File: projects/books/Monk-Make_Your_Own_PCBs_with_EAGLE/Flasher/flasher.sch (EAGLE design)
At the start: 10 parts, among them IC1 NE555, J1 1X2-3.5MM

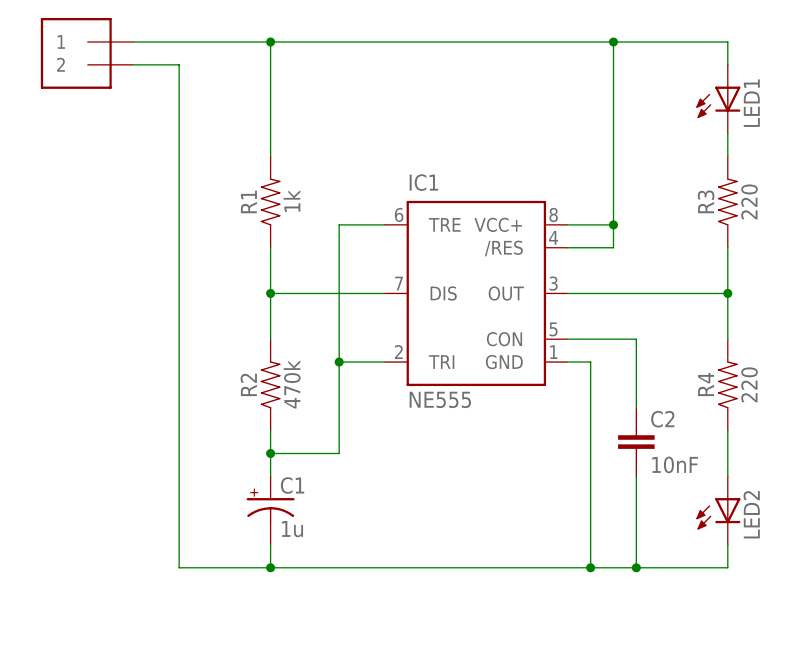
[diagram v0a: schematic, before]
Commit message: Updated flasher schematic
Signed-off-by: Naveed Kawsar <naveedkawsar@outlook.com>
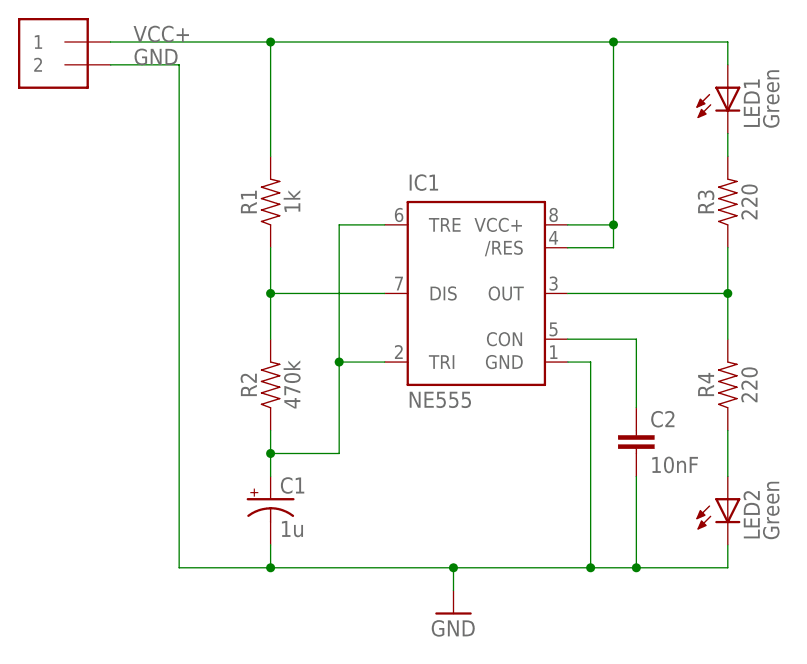
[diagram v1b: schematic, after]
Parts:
- LED1, LED2: value (none) -> Green
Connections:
- net N$5 renamed VCC+
- net N$6 renamed GND
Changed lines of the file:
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@@
 </classes>
 <parts>
-<part name="FRAME1" library="frames" library_urn="urn:adsk.eagle:library:229" deviceset="A4L-LOC" device=""/>
 <part name="R1" library="SparkFun-Resistors" deviceset="1KOHM" device="-HORIZ-1/4W-1%" value="1k"/>
 <part name="R2" library="SparkFun-Resistors" deviceset="RESISTOR" device="AXIAL-0.3" value=" 470k"/>
@@
 <part name="R4" library="SparkFun-Resistors" deviceset="220OHM" device="-0603-1/10W-1%" value="220"/>
 <part name="IC1" library="st-microelectronics" library_urn="urn:adsk.eagle:library:368" deviceset="NE555" device="" package3d_urn="urn:adsk.eagle:package:26829/1"/>
-<part name="LED1" library="led" library_urn="urn:adsk.eagle:library:259" deviceset="LED" device="5MM" package3d_urn="urn:adsk.eagle:package:15799/1"/>
-<part name="LED2" library="led" library_urn="urn:adsk.eagle:library:259" deviceset="LED" device="5MM" package3d_urn="urn:adsk.eagle:package:15799/1"/>
+<part name="LED1" library="led" library_urn="urn:adsk.eagle:library:259" deviceset="LED" device="5MM" package3d_urn="urn:adsk.eagle:package:15799/1" value="Green"/>
+<part name="LED2" library="led" library_urn="urn:adsk.eagle:library:259" deviceset="LED" device="5MM" package3d_urn="urn:adsk.eagle:package:15799/1" value="Green"/>
 <part name="C1" library="resistor" library_urn="urn:adsk.eagle:library:348" deviceset="CPOL-US" device="E2.5-5" package3d_urn="urn:adsk.eagle:package:25841/1" value="1u"/>
 <part name="J1" library="adafruit" deviceset="1X2" device="-3.5MM"/>
 <part name="C2" library="SparkFun-Capacitors" deviceset="10NF" device="-PTH-10MM-10000V-1-%" value="10nF"/>
+<part name="GND1" library="supply1" library_urn="urn:adsk.eagle:library:371" deviceset="GND" device=""/>
+<part name="FRAME1" library="frames" library_urn="urn:adsk.eagle:library:229" deviceset="FRAME_A_L" device=""/>
 </parts>
 <sheets>
@@
 </plain>
 <instances>
-<instance part="FRAME1" gate="G$1" x="-66.04" y="-55.88"/>
 <instance part="R1" gate="G$1" x="43.18" y="48.26" rot="R90"/>
 <instance part="R2" gate="G$1" x="43.18" y="27.94" rot="R90"/>
@@
 <instance part="LED2" gate="G$1" x="93.98" y="15.24"/>
 <instance part="C1" gate="G$1" x="43.18" y="15.24"/>
-<instance part="J1" gate="G$1" x="22.86" y="63.5" rot="MR0"/>
+<instance part="J1" gate="G$1" x="20.32" y="63.5" rot="MR0"/>
 <instance part="C2" gate="G$1" x="83.82" y="20.32"/>
+<instance part="GND1" gate="1" x="63.5" y="2.54"/>
+<instance part="FRAME1" gate="G$1" x="-73.66" y="-71.12"/>
+<instance part="FRAME1" gate="G$2" x="99.06" y="-71.12"/>
 </instances>
 <busses>
@@
 </segment>
 </net>
-<net name="N$6" class="0">
-<segment>
-<pinref part="C1" gate="G$1" pin="-"/>
-<wire x1="43.18" y1="10.16" x2="43.18" y2="7.62" width="0.1524" layer="91"/>
-<wire x1="43.18" y1="7.62" x2="78.74" y2="7.62" width="0.1524" layer="91"/>
-<pinref part="LED2" gate="G$1" pin="C"/>
-<wire x1="78.74" y1="7.62" x2="83.82" y2="7.62" width="0.1524" layer="91"/>
-<wire x1="83.82" y1="7.62" x2="93.98" y2="7.62" width="0.1524" layer="91"/>
-<wire x1="93.98" y1="7.62" x2="93.98" y2="10.16" width="0.1524" layer="91"/>
-<pinref part="IC1" gate="G$1" pin="GND"/>
-<wire x1="76.2" y1="30.48" x2="78.74" y2="30.48" width="0.1524" layer="91"/>
-<wire x1="78.74" y1="30.48" x2="78.74" y2="7.62" width="0.1524" layer="91"/>
-<junction x="78.74" y="7.62"/>
-<pinref part="J1" gate="G$1" pin="2"/>
-<wire x1="27.94" y1="63.5" x2="33.02" y2="63.5" width="0.1524" layer="91"/>
-<wire x1="33.02" y1="63.5" x2="33.02" y2="7.62" width="0.1524" layer="91"/>
-<wire x1="33.02" y1="7.62" x2="43.18" y2="7.62" width="0.1524" layer="91"/>
-<junction x="43.18" y="7.62"/>
-<pinref part="C2" gate="G$1" pin="2"/>
-<wire x1="83.82" y1="17.78" x2="83.82" y2="7.62" width="0.1524" layer="91"/>
-<junction x="83.82" y="7.62"/>
-</segment>
-</net>
 <net name="N$7" class="0">
 <segment>
@@
 </segment>
 </net>
-<net name="N$5" class="0">
+<net name="VCC+" class="0">
 <segment>
 <pinref part="LED1" gate="G$1" pin="A"/>
@@
 <junction x="81.28" y="45.72"/>
 <pinref part="J1" gate="G$1" pin="1"/>
-<wire x1="27.94" y1="66.04" x2="43.18" y2="66.04" width="0.1524" layer="91"/>
+<wire x1="25.4" y1="66.04" x2="43.18" y2="66.04" width="0.1524" layer="91"/>
 <junction x="43.18" y="66.04"/>
+<label x="27.94" y="66.04" size="1.778" layer="95"/>
 </segment>
 </net>
@@
 </segment>
 </net>
+<net name="GND" class="0">
+<segment>
+<pinref part="C1" gate="G$1" pin="-"/>
+<wire x1="43.18" y1="10.16" x2="43.18" y2="7.62" width="0.1524" layer="91"/>
+<wire x1="43.18" y1="7.62" x2="63.5" y2="7.62" width="0.1524" layer="91"/>
+<pinref part="LED2" gate="G$1" pin="C"/>
+<wire x1="63.5" y1="7.62" x2="78.74" y2="7.62" width="0.1524" layer="91"/>
+<wire x1="78.74" y1="7.62" x2="83.82" y2="7.62" width="0.1524" layer="91"/>
+<wire x1="83.82" y1="7.62" x2="93.98" y2="7.62" width="0.1524" layer="91"/>
+<wire x1="93.98" y1="7.62" x2="93.98" y2="10.16" width="0.1524" layer="91"/>
+<pinref part="IC1" gate="G$1" pin="GND"/>
+<wire x1="76.2" y1="30.48" x2="78.74" y2="30.48" width="0.1524" layer="91"/>
+<wire x1="78.74" y1="30.48" x2="78.74" y2="7.62" width="0.1524" layer="91"/>
+<junction x="78.74" y="7.62"/>
+<pinref part="J1" gate="G$1" pin="2"/>
+<wire x1="25.4" y1="63.5" x2="33.02" y2="63.5" width="0.1524" layer="91"/>
+<wire x1="33.02" y1="63.5" x2="33.02" y2="7.62" width="0.1524" layer="91"/>
+<wire x1="33.02" y1="7.62" x2="43.18" y2="7.62" width="0.1524" layer="91"/>
+<junction x="43.18" y="7.62"/>
+<pinref part="C2" gate="G$1" pin="2"/>
+<wire x1="83.82" y1="17.78" x2="83.82" y2="7.62" width="0.1524" layer="91"/>
+<junction x="83.82" y="7.62"/>
+<pinref part="GND1" gate="1" pin="GND"/>
+<wire x1="63.5" y1="5.08" x2="63.5" y2="7.62" width="0.1524" layer="91"/>
+<junction x="63.5" y="7.62"/>
+<label x="27.94" y="63.5" size="1.778" layer="95"/>
+</segment>
+</net>
